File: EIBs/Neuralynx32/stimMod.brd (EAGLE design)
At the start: 18 x 18 mm, 41 parts, among them CON1 A79022-001_MALESMD

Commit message: Updated stim board
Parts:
- moved STIM2_2 0.46 mm to (17.3, 6.81)
- moved STIM1_2 0.38 mm to (3.33, 7.01)
- moved STIM2_1 0.28 mm to (17.3, 9.22)
- moved R2 0.18 mm to (17.7, 12.8)
- moved G2 0.16 mm to (18.0, 10.1)
- moved 3.4 0.13 mm to (15.3, 5.41)
- moved 2.3 0.10 mm to (11.2, 4.90)
- moved 2.2 0.10 mm to (9.54, 4.90)
- moved STIM1_1 0.08 mm to (2.97, 8.48)
- moved 4.2 0.05 mm to (15.9, 13.4)
- moved R1 0.05 mm to (3.14, 12.8)
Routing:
- net N$35: track 9.18 -> 11.4 mm
- net GND: track 117.6 -> 115.4 mm
- net N$4: track 10.8 -> 12.5 mm
- net N$22: track 11.9 -> 13.1 mm
- net N$33: track 1.17 -> 0.00 mm
- net N$41: track 0.00 -> 0.97 mm
- net N$39: track 0.00 -> 0.94 mm
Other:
- board size 18 x 18 mm -> 19 x 19.1 mm

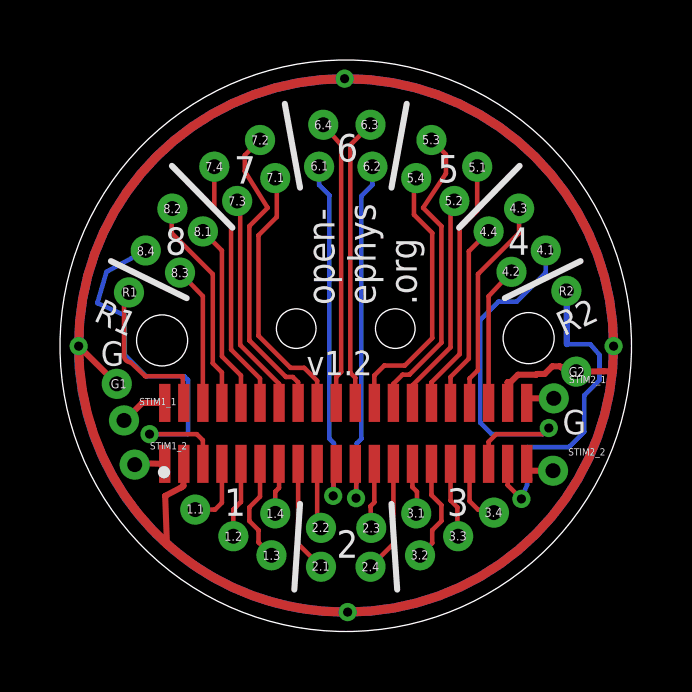
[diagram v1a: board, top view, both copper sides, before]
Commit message: Updated design to fix error
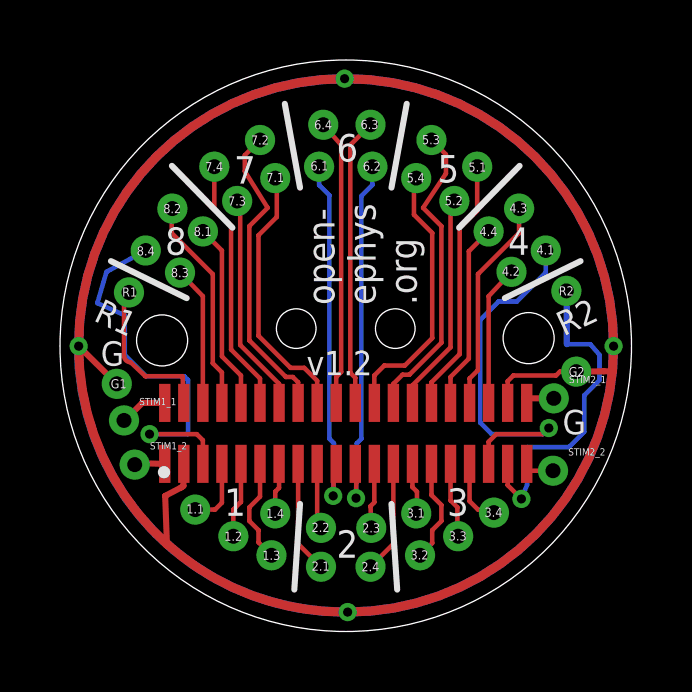
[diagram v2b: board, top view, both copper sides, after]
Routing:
- net N$39: track 0.94 -> 0.00 mm
- net N$33: track 0.00 -> 0.81 mm
- net N$36: track 0.77 -> 0.00 mm
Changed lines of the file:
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@@
 <?xml version="1.0" encoding="utf-8"?>
 <!DOCTYPE eagle SYSTEM "eagle.dtd">
-<eagle version="8.0.0">
+<eagle version="7.7.0">
 <drawing>
 <settings>
@@
 <wire x1="10.31221875" y1="19.888428125" x2="10.324665625" y2="19.87546875" width="0.2032" layer="1"/>
 <via x="1.460065625" y="10.96006875" extent="1-16" drill="0.3048"/>
-<wire x1="15.76051875" y1="9.068028125" x2="15.76051875" y2="9.7536" width="0.2032" layer="1"/>
-<wire x1="15.76051875" y1="9.7536" x2="15.76051875" y2="9.76611875" width="0.2032" layer="1"/>
 <wire x1="4.96551875" y1="7.036028125" x2="4.953" y2="7.277509375" width="0.2032" layer="1"/>
 <wire x1="4.953" y1="7.277509375" x2="4.953" y2="6.2992" width="0.2032" layer="1"/>
@@
 <wire x1="4.8768" y1="6.2484" x2="4.3434" y2="5.969" width="0.2032" layer="1"/>
 <wire x1="4.3434" y1="5.969" x2="4.40266875" y2="4.363775" width="0.2032" layer="1"/>
-<wire x1="15.8496" y1="9.7536" x2="16.1036" y2="10.0076" width="0.2032" layer="1"/>
-<wire x1="15.8496" y1="9.7536" x2="15.76051875" y2="9.7536" width="0.2032" layer="1"/>
-<wire x1="17.2466" y1="10.287" x2="17.5006" y2="10.287" width="0.2032" layer="1"/>
-<wire x1="16.9926" y1="10.033" x2="17.2466" y2="10.287" width="0.2032" layer="1"/>
-<wire x1="16.7386" y1="10.033" x2="16.9926" y2="10.033" width="0.2032" layer="1"/>
-<wire x1="16.7132" y1="10.0076" x2="16.7386" y2="10.033" width="0.2032" layer="1"/>
-<wire x1="16.1036" y1="10.0076" x2="16.7132" y2="10.0076" width="0.2032" layer="1"/>
-<wire x1="17.5768" y1="10.2362" x2="18.1356" y2="10.2362" width="0.2032" layer="1"/>
-<wire x1="18.1356" y1="10.2362" x2="18.04651875" y2="10.109428125" width="0.2032" layer="1"/>
-<wire x1="17.5768" y1="10.2362" x2="17.5006" y2="10.287" width="0.2032" layer="1"/>
 <wire x1="18.960709375" y1="10.121259375" x2="19.290865625" y2="10.121259375" width="0.2032" layer="1"/>
 <wire x1="19.290865625" y1="10.121259375" x2="19.290865625" y2="10.96006875" width="0.2032" layer="1"/>
+<wire x1="15.76051875" y1="9.195028125" x2="15.76051875" y2="9.79151875" width="0.1524" layer="1"/>
+<wire x1="18.04651875" y1="10.109428125" x2="17.500828125" y2="10.109428125" width="0.1524" layer="1"/>
+<wire x1="17.500828125" y1="10.109428125" x2="17.3736" y2="9.9822" width="0.1524" layer="1"/>
+<wire x1="17.3736" y1="9.9822" x2="15.9512" y2="9.9822" width="0.1524" layer="1"/>
+<wire x1="15.9512" y1="9.9822" x2="15.76051875" y2="9.79151875" width="0.1524" layer="1"/>
 </signal>
 <signal name="N$97">
@@
 <wire x1="13.70311875" y1="17.348428125" x2="13.22051875" y2="17.831028125" width="0.1524" layer="1"/>
 </signal>
-<signal name="N$33">
-<wire x1="17.5514" y1="9.1694" x2="17.4752" y2="9.2456" width="0" layer="19" extent="1-16"/>
-<wire x1="17.4752" y1="9.2456" x2="16.4084" y2="9.2456" width="0" layer="19" extent="1-16"/>
-</signal>
-<signal name="N$36">
-<wire x1="16.4846" y1="6.5024" x2="16.383" y2="7.2644" width="0.2032" layer="1"/>
-</signal>
 <signal name="N$37">
 <wire x1="2.9718" y1="8.4582" x2="3.5814" y2="9.0678" width="0.2032" layer="1"/>
@@
 </signal>
 <signal name="N$39">
-<wire x1="17.2466" y1="6.8072" x2="16.4338" y2="6.8072" width="0.2032" layer="1"/>
-<wire x1="16.4338" y1="6.8072" x2="16.4338" y2="6.9342" width="0.2032" layer="1"/>
-</signal>
-<signal name="N$40">
-<wire x1="16.4084" y1="9.2456" x2="16.5354" y2="9.2456" width="0" layer="19" extent="1-16"/>
-<wire x1="16.5354" y1="9.2456" x2="17.272" y2="9.2456" width="0" layer="19" extent="1-16"/>
-<wire x1="16.4084" y1="9.2456" x2="16.383" y2="9.2456" width="0" layer="19" extent="1-16"/>
+<wire x1="16.4338" y1="6.8072" x2="16.4338" y2="6.9342" width="0" layer="19" extent="1-16"/>
 </signal>
 <signal name="N$41">
 <wire x1="16.3068" y1="9.2202" x2="17.272" y2="9.2202" width="0.2032" layer="1"/>
 </signal>
+<signal name="N$33">
+<wire x1="17.2466" y1="6.8072" x2="16.4338" y2="6.8072" width="0.1524" layer="1"/>
+</signal>
 </signals>
